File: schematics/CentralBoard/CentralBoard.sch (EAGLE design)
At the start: 10 parts, among them CON1 XT30UPB-M, CON3 XT30UPB-M, IC1 7805T

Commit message: Starting schematics
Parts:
- removed JP1: OD0_Serial, adafruit:PINHD-1X3
- added C10, C11, C12, C13, C14, C15, C9: 2.2uF, rcl:C-EUC1206
- added C17, C2, C4, C7: 100nF, rcl:C-EUC0805
- added CON2, CON4, CON5, CON6, CON7, CON8: XT30UPB-M, amass:XT30UPB-M
- added F1: Fuse 0.2A, fuse:FUSESHK20L
- added IC2: SN75C3232, MAX3232:MAX3232
- added IC3: LTC7001, LTC7001:LTC7001
- added Q1: BC328, transistor-pnp:BC328
- added R3: 4m, rcl:R-EU_R2512
- added R4: 10K, rcl:R-EU_R0805
- added R5: 100K, rcl:R-EU_R0805
- added R6, R7: 1K, rcl:R-EU_R0805
- added SJ1, SJ2, SJ3, SJ4: 0, jumper:SJ
- added SV3: IMU, con-lstb:MA06-1
- added U$2: NVMFS6H824NL-D, DIO_NTS1045EMFST1G:NVMFS6H824NL-D
- C1: value (none) -> 1uF; device rcl:CPOL-EUE15-5AXIAL -> rcl:CPOL-EUE2-5
- C3: value (none) -> 4.7uF; device rcl:CPOL-EUE15-5AXIAL -> rcl:C-EUC0805
- C5: value (none) -> 10uF; device rcl:CPOL-EUE2.5-7 -> rcl:CPOL-EUE2-5
- C6: value (none) -> 0.47uF; device rcl:CPOL-EUE2.5-7 -> rcl:C-EUC0805
- D1: device adafruit:1N4004 -> diode:1N4004
- IC1: value 7805T -> R-78C05.0; device adafruit:7805T -> v-reg:78XXS
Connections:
- removed net RX1: JP1.1, U$1.0-RX1/CS1/CRX2
- removed net TX1: JP1.2, U$1.1-TX1/MISO1/CTX2
- new net +5V: C5.+, D1.A, IC1.OUT, IC3.VCC, Q1.E, R6.1, U$1.VIN
- new net BATT+: CON1.+, CON3.+, R3.1, SJ1.1
- new net BATT-: C10.2, C11.2, C12.2, C13.2, C14.2, C15.2, C9.2, CON1.-, CON2.-, CON3.-, CON4.-, CON5.-, CON6.-, CON7.-, CON8.-, SJ2.1, SJ4.2
- new net IMU-D+: SV3.4
- new net IMU_D-: SV3.3
- new net IMU_RX: IC2.T1OUT, SV3.6
- new net IMU_TX: IC2.R1IN, SV3.5
- new net IMU_VDD: Q1.C, SV3.2
- new net N$1: C1.+, D1.C, F1.2, IC1.IN
- new net N$10: IC3.INP, R4.2, U$1.30-CRX3
- new net N$11: C2.1, IC2.C2+
- new net N$12: C2.2, IC2.C2-
- new net N$13: C7.1, IC2.V+
- new net N$14: C4.1, IC2.V-
- new net N$15: R4.1, SJ4.1
- new net N$16: C3.1, IC3.BST
- new net N$17: IC3.TGUP, R5.2
- new net N$18: R3.2, U$2.D
- new net N$19: C6.1, IC3.TGDN, R5.1, U$2.G
- new net N$2: IC2.T1IN, U$1.29-TX7
- new net N$20: F1.1, SJ1.2
- new net N$21: C10.1, C11.1, C12.1, C13.1, C14.1, C15.1, C9.1, CON2.+, CON4.+, CON5.+, CON6.+, CON7.+, CON8.+, SJ3.2, U$2.S
- new net N$5: IC2.R1OUT, U$1.28-RX7
- new net N$6: C17.1, IC2.C1+
- new net N$7: R6.2, R7.1, U$1.10-CS/MQSR
- new net N$8: C17.2, IC2.C1-
- new net N$9: IC2.VCC, U$1.3V3-3
- net GND: now also C4.2, C7.2, IC2.GND, IC3.GND, IC3.OVLO, IC3.VCCUV, SJ2.2, SV3.1; no longer C3.-, C6.-, CON1.-, CON3.-, JP1.3
- net N$3: now also Q1.B, R7.2; no longer C1.+, C5.+, D1.A, IC1.VO, U$1.VIN
- net N$4: now also C3.2, C6.2, IC3.TS, SJ3.1; no longer C3.+, C6.+, CON1.+, CON3.+, D1.C, IC1.VI
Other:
- moved on the sheet: C1, C5, CON1, CON3

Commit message: used MAX3232 IC for IMU connection now
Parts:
- removed C3: 4.7uF, rcl:C-EUC0805
- removed F1: Fuse 0.2A, fuse:FUSESHK20L
- removed IC3: LTC7001, LTC7001:LTC7001
- removed R5: 100K, rcl:R-EU_R0805
- removed R6: 1K, rcl:R-EU_R0805
- added D2: 1N4148DO35-7, diode:1N4148DO35-7
- added R1: 10k, rcl:R-EU_R0805
- added U1: LTC4440ES6-5TRMSOP8P, LTC4440ES6-5TR:LTC4440ES6-5TRMSOP8P
- U$2: value NVMFS6H824NL-D -> DMTH8003SPS
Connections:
- removed net N$16: C3.1, IC3.BST
- removed net N$17: IC3.TGUP, R5.2
- new net N$24: C6.1, D2.C, U1.BOOST
- net +5V: now also D2.A, R1.1, U1.VCC; no longer IC3.VCC, R6.1
- net GND: no longer IC3.GND, IC3.OVLO, IC3.VCCUV
- net N$1: no longer F1.2
- net N$10: now also U1.INP; no longer IC3.INP
- net N$15: now also U1.GND
- net N$19: now also U1.TG; no longer C6.1, IC3.TGDN, R5.1
- net N$20: no longer F1.1
- net N$3: now also R1.2
- net N$4: now also U1.TS; no longer C3.2, IC3.TS
- net N$7: now also U$1.9-OUT1C; no longer R6.2, U$1.10-CS/MQSR
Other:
- moved on the sheet: Q1, R4, R7

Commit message: Added sockets for IMU, Sensors and ODrives
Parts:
- removed D1: 1N4004, diode:1N4004
- removed IC1: R-78C05.0, v-reg:78XXS
- removed Q1: BC328, transistor-pnp:BC328
- removed SV3: IMU, con-lstb:MA06-1
- removed U1: LTC4440ES6-5TRMSOP8P, LTC4440ES6-5TR:LTC4440ES6-5TRMSOP8P
- added C3: 4.7uF, rcl:C-EUC0805
- added C8: 10uF, rcl:C-EUC0805
- added IC3: LTC7001, LTC7001:LTC7001
- added L1: 10uH, rcl:L-EU0204/5
- added LED1: Power, led:LG_T679-E1F1-1
- added LED2: P-ODrive, led:LG_T679-E1F1-1
- added P10: Power Switch, jst-ph:JST-PH2
- added P11: Foot4, jst-ph:JST-PH3
- added P12: Foot3, jst-ph:JST-PH3
- added P13: Foot2, jst-ph:JST-PH3
- added P14: Foot1, jst-ph:JST-PH3
- added P2: ODrive1, jst-ph:JST-PH3
- added P3: MAIN_SPI, jst-ph:JST-PH4
- added P4: IMU, jst-ph:JST-PH6
- added P5: ODrive2, jst-ph:JST-PH3
- added P6: ODrive3, jst-ph:JST-PH3
- added P7: ODrive4, jst-ph:JST-PH3
- added P8: ODrive5, jst-ph:JST-PH3
- added P9: ODrive6, jst-ph:JST-PH3
- added R10: 100k, rcl:R-EU_R0805
- added R11, R8: 100K, rcl:R-EU_R0805
- added R12, R13: 1K, rcl:R-EU_R0805
- added R2, R5: 2.2K, rcl:R-EU_R0805
- added R6: 10K, rcl:R-EU_R0805
- added R9: 47k, rcl:R-EU_R0805
- added SJ5: 0, jumper:SJ
- added U$3: TLF50211EL, TLF50211EL:TLF50211EL
- added U$4: MCP1725-ADJE/SN, MCP1725-ADJE_SN:MCP1725-ADJE/SN
- added U$5: AP2128-3.3V, AP2128:AP2128-3.3V
- added U2: INA226AIDGST, INA226AIDGST:INA226AIDGST
- C1: device rcl:CPOL-EUE2-5 -> rcl:C-EUC0805
- C5: value 10uF -> 1nF; device rcl:CPOL-EUE2-5 -> rcl:C-EUC0805
- D2: value 1N4148DO35-7 -> 1N4004; device diode:1N4148DO35-7 -> diode:1N4004
- R1: value 10k -> 100K
- R7: value 1K -> 10K
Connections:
- net N$2 renamed T_TX
- net N$5 renamed T_RX
- new net +3.3V: C1.1, P11.2, P12.2, P13.2, P14.2, U$5.OUT
- new net BATT: P10.1, SJ1.2, U$3.VS, U2.IN+, U2.VBUS
- new net CS: P3.4, U$1.10-CS/MQSR
- new net MISO: P3.2, U$1.12-MISO/MQSL
- new net MOSI: P3.3, U$1.11-MOSI/CTX1
- new net N$16: C6.2, R6.2
- new net N$17: R2.1, U$1.19-A5/SCL0, U2.SCL
- new net N$2: LED1.C, R12.2
- new net N$22: R5.1, U$1.18-A4/SDA0, U2.SDA
- new net N$23: R11.2, R2.2, R5.2, U$1.3V3-3, U2.VS
- new net N$25: R1.1, R7.2, U$4.ADJ
- new net N$26: C3.2, IC3.TS, LED2.A, SJ3.1
- new net N$27: R9.2, U$3.FREQ
- new net N$29: D2.C, L1.1, U$3.SWO
- new net N$30: LED2.C, R13.2
- new net N$31: IC2.VCC, P4.5, R1.2, U$4.VOUT
- new net N$5: U$1.31-CTX3, U2.ALERT
- new net O1_RX: P2.2, U$1.0-RX1/CS1/CRX2
- new net O1_TX: P2.3, U$1.1-TX1/MISO1/CTX2
- new net O2_RX: P5.2, U$1.7-RX2/OUT1A
- new net O2_TX: P5.3, U$1.8-TX2/IN1
- new net O3_RX: P6.2, U$1.15-A1/RX3/SPDIF_IN
- new net O3_TX: P6.3, U$1.14-A0/TX3/SPDIF_OUT
- new net O4_RX: P7.2, U$1.16-A2/RX4/SCL1
- new net O4_TX: P7.3, U$1.17-A3/TX4/SDA1
- new net O5_RX: P8.2, U$1.21-A7/RX5/BCLK1
- new net O5_TX: P8.3, U$1.20-A6/TX5/LRCLK1
- new net O6_RX: P9.2, U$1.25-A11/RX6/SDA2
- new net O6_TX: P9.3, U$1.24-A10/TX6/SCL2
- new net SENSOR1: P14.3, U$1.22-A8/CTX1
- new net SENSOR2: P13.3, U$1.23-A9/CRX1/MCLK1
- new net SENSOR3: P12.3, U$1.38-A14/CS/IN1
- new net SENSOR4: P11.3, U$1.39-A15/CS/OUT1A
- net +5V: now also C8.1, IC3.VCC, L1.2, LED1.A, U$3.FB, U$4.VIN, U$5.IN; no longer C5.+, D1.A, D2.A, IC1.OUT, Q1.E, R1.1, U$1.VIN, U1.VCC
- net GND: now also C1.2, C5.2, C8.2, D2.A, P11.1, P12.1, P13.1, P14.1, P2.1, P3.1, P4.6, P5.1, P6.1, P7.1, P8.1, P9.1, R10.1, R12.1, R7.1, R9.1, U$3.GND, U$3.SYNC, U$4.GND, U$5.GND, U2.A0, U2.A1, U2.GND; no longer C1.-, C5.-, IC1.GND, SV3.1
- net IMU-D+: now also P4.3; no longer SV3.4
- net IMU_D-: now also P4.4; no longer SV3.3
- net IMU_RX: now also P4.1; no longer SV3.6
- net IMU_TX: now also P4.2; no longer SV3.5
- net IMU_VDD: now also R11.1, U$1.32-OUT1B, U$4.PWRGD; no longer Q1.C, SV3.2
- net N$1: now also U$1.VIN; no longer C1.+, D1.C, IC1.IN
- net N$10: now also IC3.INP; no longer U1.INP
- net N$15: now also IC3.GND, IC3.OVLO, IC3.VCCUV, R13.1, R6.1; no longer U1.GND
- net N$18: now also SJ5.1, U2.IN-; no longer R3.2, U$2.D
- net N$19: now also C6.1, IC3.TGDN, R8.1; no longer U1.TG
- net N$20: now also P10.2, R10.2, U$3.EN; no longer SJ1.2
- net N$24: now also C3.1, IC3.BST; no longer C6.1, D2.C, U1.BOOST
- net N$3: now also C5.1, U$4.CDELAY; no longer Q1.B, R1.2, R7.2
- net N$4: now also IC3.TGUP, R8.2; no longer C6.2, SJ3.1, U1.TS
- net N$7: now also U$4.!SHDN; no longer R7.1
- net N$9: now also R3.2, SJ5.2, U$2.D; no longer IC2.VCC, U$1.3V3-3
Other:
- moved on the sheet: C6, CON1, CON3, R1, R3, R7, SJ1, SJ2

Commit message: removed old SMD version
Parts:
- removed C1: 1uF, rcl:C-EUC0805
- removed C5: 1nF, rcl:C-EUC0805
- removed C8: 10uF, rcl:C-EUC0805
- removed D2: 1N4004, diode:1N4004
- removed LED1: Power, led:LG_T679-E1F1-1
- removed LED2: P-ODrive, led:LG_T679-E1F1-1
- removed R9: 47k, rcl:R-EU_R0805
- added C16: 2.2uF, rcl:CPOL-EUE2-5
- added C18: 100nF, rcl:C-EU025-025X050
- added C19: 4.7uF, rcl:C-EU025-025X050
- added D1: (no value), adafruit:SCHOTTKY-DIODEDO41
- added LED3: P-ODrive, adafruit:LED3MM
- added LED4: ON, adafruit:LED3MM
- added P1: Foot1, jst-ph:JST-PH3
- added R15: 1k, rcl:R-EU_0204/7
- C10, C11, C12, C13, C14, C9: device rcl:C-EUC1206 -> rcl:CPOL-EUE2-5
- C15: value 2.2uF -> 0.47uF#; device rcl:C-EUC1206 -> rcl:C-EU025-025X050
- C17: value 100nF -> 10uF; device rcl:C-EUC0805 -> rcl:CPOL-EUE2-4
- C2, C4: device rcl:C-EUC0805 -> rcl:C-EU025-025X050
- C3: value 4.7uF -> 100nF; device rcl:C-EUC0805 -> rcl:C-EU025-025X050
- C6: value 0.47uF -> 1uF; device rcl:C-EUC0805 -> rcl:CPOL-EUE2-4
- C7: value 100nF -> 1nF; device rcl:C-EUC0805 -> rcl:C-EU025-025X050
- P10: value Power Switch -> Switch
- P11: value Foot4 -> Foot2
- P13: value Foot2 -> Foot4
- P14: value Foot1 -> SPI2; device jst-ph:JST-PH3 -> jst-ph:JST-PH4
- P3: value MAIN_SPI -> SPI
- R1: value 100K -> 10K; device rcl:R-EU_R0805 -> rcl:R-EU_0204/7
- R10, R13, R2, R5: device rcl:R-EU_R0805 -> rcl:R-EU_0204/7
- R11: value 100K -> 100k; device rcl:R-EU_R0805 -> rcl:R-EU_0204/7
- R12: value 1K -> 100k; device rcl:R-EU_R0805 -> rcl:R-EU_0204/7
- R4: value 10K -> 10k; device rcl:R-EU_R0805 -> rcl:R-EU_0204/7
- R6: value 10K -> 100k; device rcl:R-EU_R0805 -> rcl:R-EU_0204/7
- R7: value 10K -> 47k; device rcl:R-EU_R0805 -> rcl:R-EU_0204/7
- R8: value 100K -> 10; device rcl:R-EU_R0805 -> rcl:R-EU_0204/7
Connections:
- net SENSOR3 renamed SENS3
- removed net SENSOR1: P14.3, U$1.22-A8/CTX1
- removed net SENSOR2: P13.3, U$1.23-A9/CRX1/MCLK1
- removed net SENSOR4: P11.3, U$1.39-A15/CS/OUT1A
- new net CS1: P14.4, U$1.40-A16/CS1
- new net MISO1: P14.2, U$1.41-A17/MISO1
- new net MOSI1: P14.3, U$1.26-A12/MOSI1
- new net SCK1: U$1.27-A13/SCK1
- new net SENS1: P1.3, U$1.22-A8/CTX1
- new net SENS2: P11.3, U$1.23-A9/CRX1/MCLK1
- new net SENS4: P13.3, U$1.39-A15/CS/OUT1A
- net +3.3V: now also C6.+, P1.2; no longer C1.1, P14.2
- net +5V: now also C17.+, LED4.A; no longer C8.1, LED1.A
- net BATT-: now also C10.-, C11.-, C12.-, C13.-, C14.-, C16.-, C9.-; no longer C10.2, C11.2, C12.2, C13.2, C14.2, C15.2, C9.2
- net GND: now also C17.-, C3.2, C6.-, D1.A, P1.1, R1.2, R13.2; no longer C1.2, C5.2, C8.2, D2.A, R10.1, R9.1
- net IMU_VDD: now also R6.1; no longer R11.1
- net N$10: now also R4.1; no longer R4.2
- net N$13: now also C4.1; no longer C7.1
- net N$14: now also C3.1; no longer C4.1
- net N$15: now also R15.2, R4.2, R8.2; no longer R13.1, R4.1, R6.1
- net N$16: now also C15.2, R8.1; no longer C6.2, R6.2
- net N$17: now also R5.2; no longer R2.1
- net N$19: now also C15.1, R10.2; no longer C6.1, R8.1
- net N$2: now also LED4.C, R13.1; no longer LED1.C, R12.2
- net N$20: now also R12.2; no longer R10.2
- net N$21: now also C10.+, C11.+, C12.+, C13.+, C14.+, C16.+, C9.+; no longer C10.1, C11.1, C12.1, C13.1, C14.1, C15.1, C9.1
- net N$22: now also R2.2; no longer R5.1
- net N$23: now also R2.1, R5.1, R6.2; no longer R11.2, R2.2, R5.2
- net N$24: now also C19.1; no longer C3.1
- net N$25: now also R11.2; no longer R7.2
- net N$26: now also C19.2, LED3.A; no longer C3.2, LED2.A
- net N$27: now also R7.2; no longer R9.2
- net N$29: now also D1.C; no longer D2.C
- net N$3: now also C7.1; no longer C5.1
- net N$30: now also LED3.C, R15.1; no longer LED2.C, R13.2
- net N$31: now also R11.1; no longer R1.2
- net N$4: now also R10.1; no longer R8.2
- net N$6: now also C18.1; no longer C17.1
- net N$8: now also C18.2; no longer C17.2
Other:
- note added: "Foot Sensor, coming in as analogue input"
- note added: "Serial connection to 6 ODrives"
- moved on the sheet: C15, C3, C4, C7, P11, P12, P13, R1, R10, R11, R12, R13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

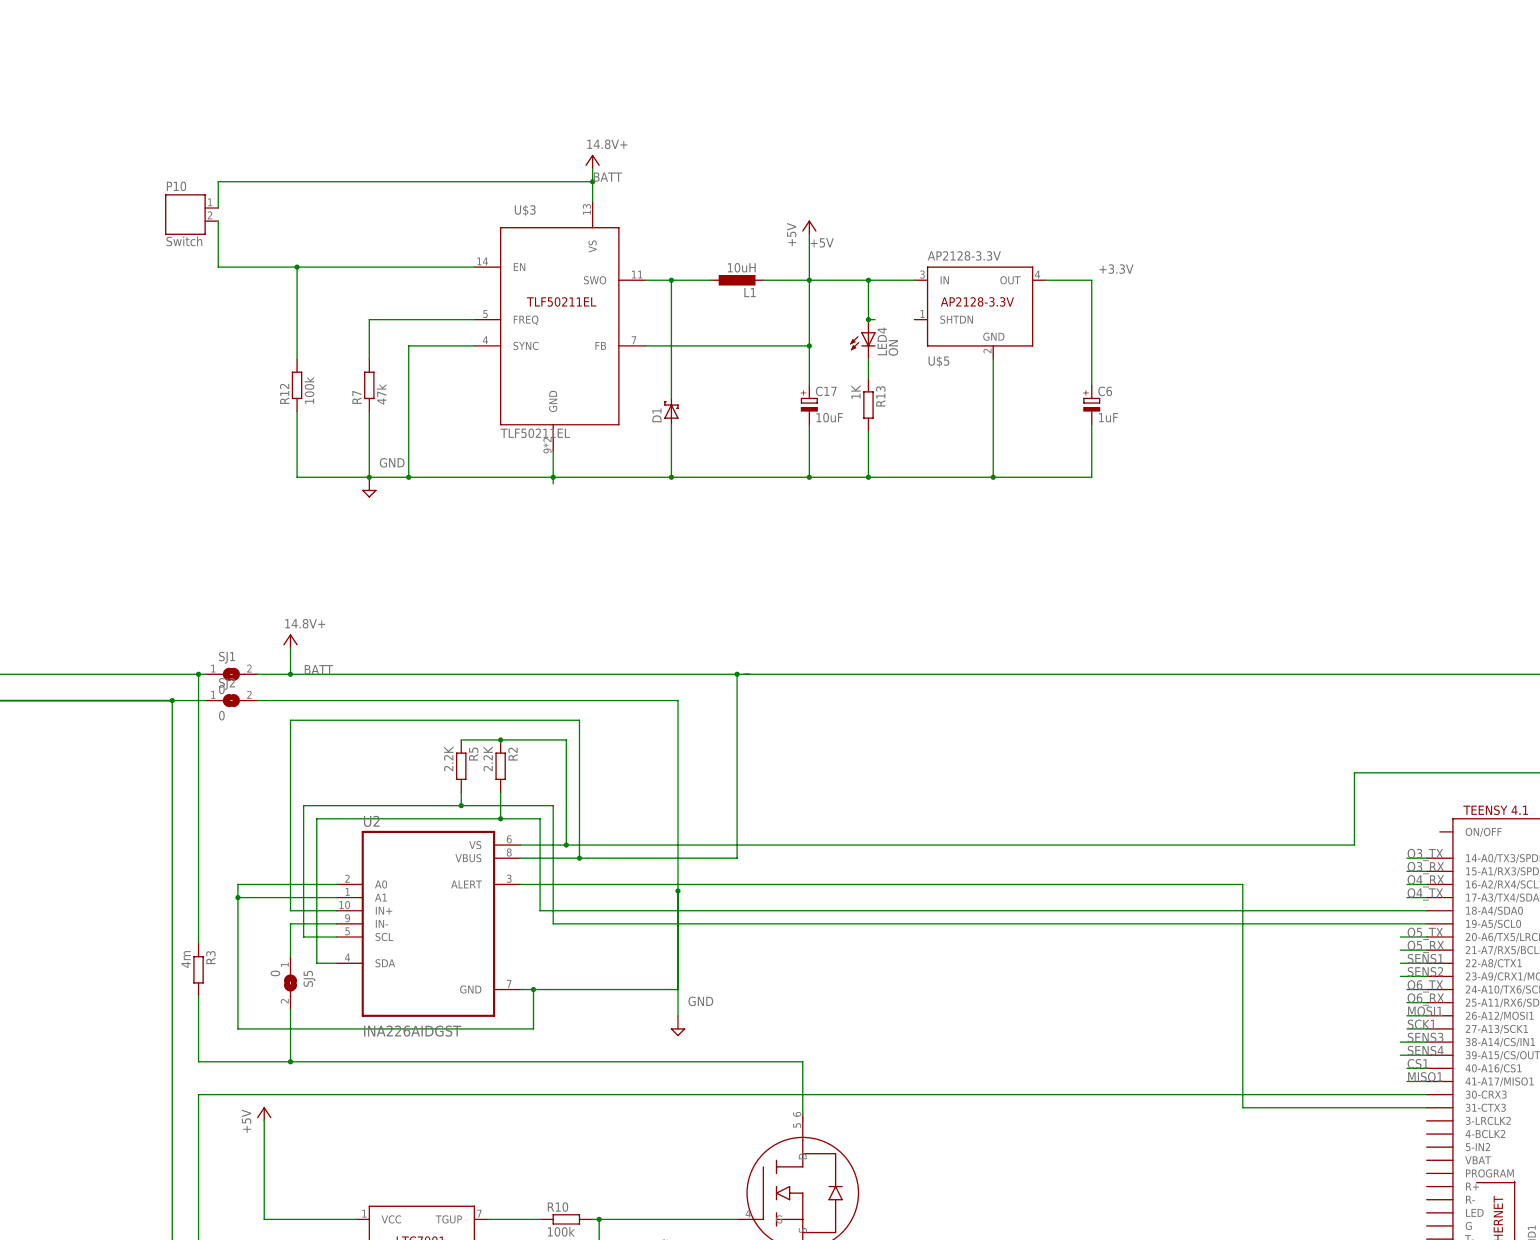
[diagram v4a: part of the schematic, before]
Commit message: new head and tail
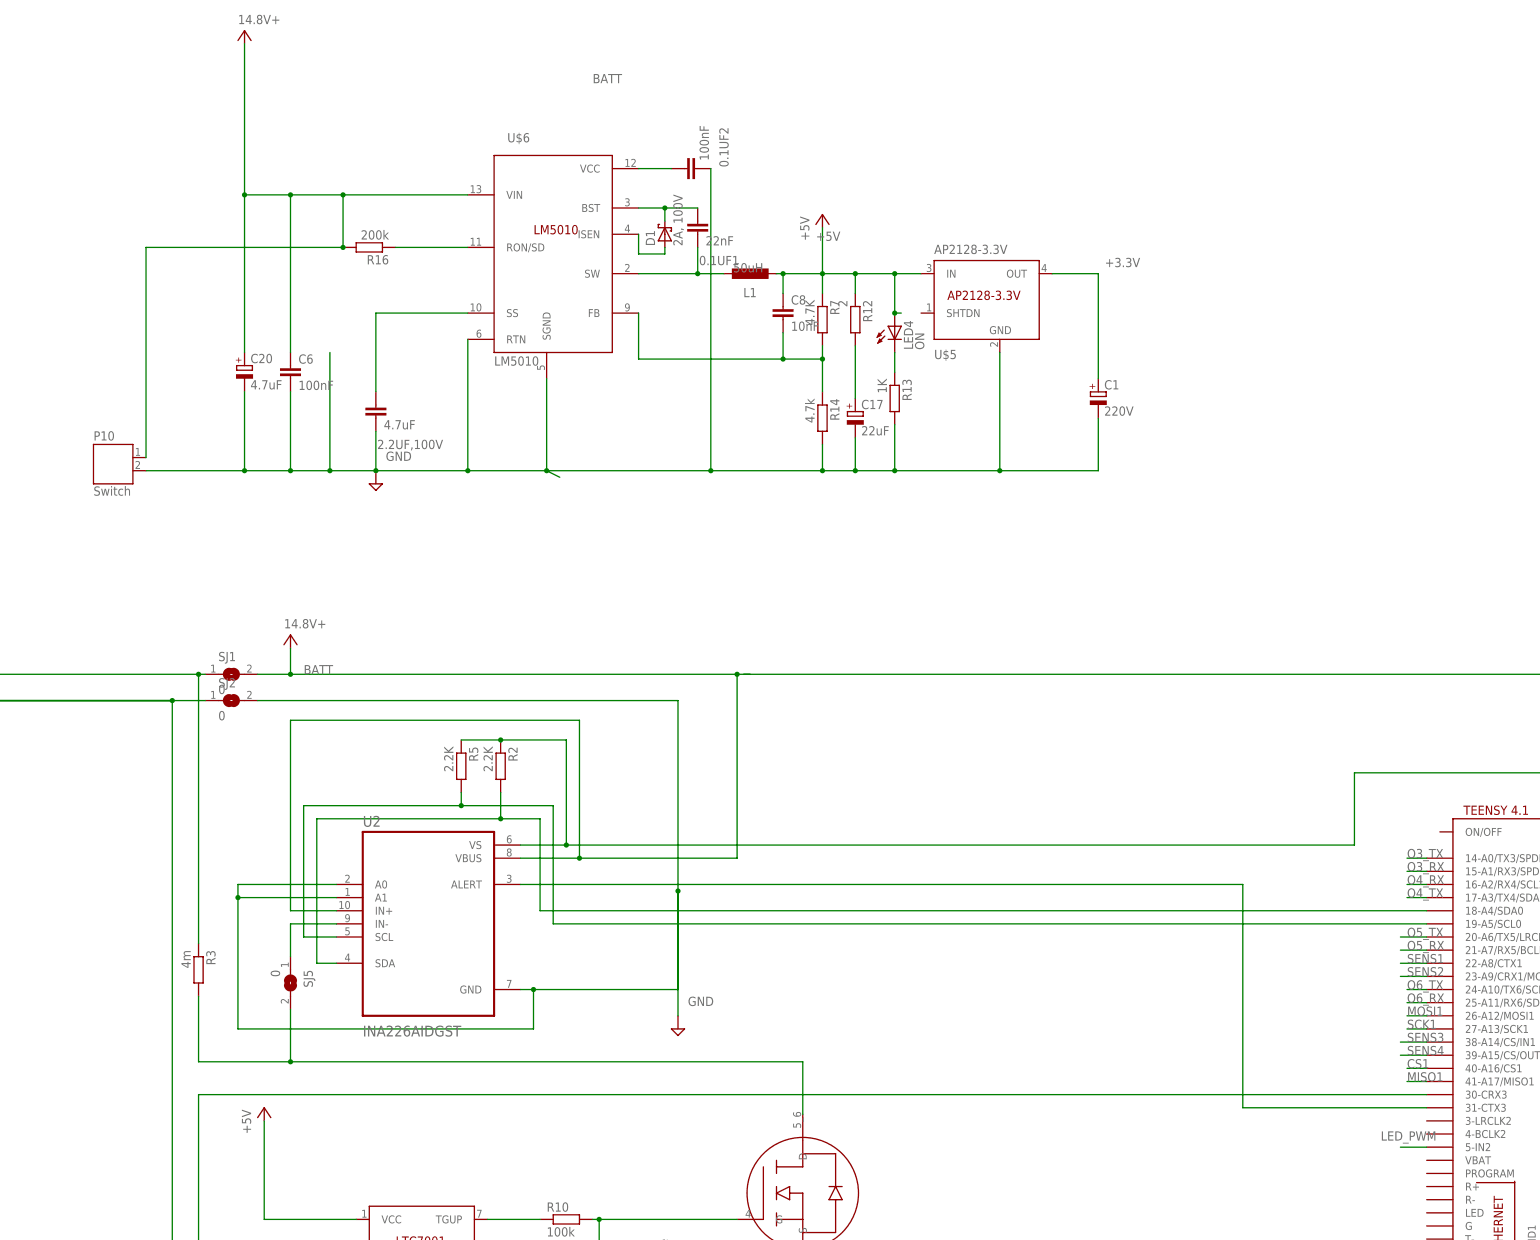
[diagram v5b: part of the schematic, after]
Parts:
- removed U$3: TLF50211EL, TLF50211EL:TLF50211EL
- added 0.1UF1: 22nF, rcl:C-EU025-025X050
- added 0.1UF2: 100nF, rcl:C-EU025-025X050
- added 2.2UF,100V: 4.7uF, rcl:C-EU025-025X050
- added C1: 220V, rcl:CPOL-EUE2.5-7
- added C20: 4.7uF, rcl:CPOL-EUE2-4
- added C8: 10nF, rcl:C-EU025-025X050
- added R14: 4.7k, rcl:R-EU_0204/7
- added R16: 200k, rcl:R-EU_0204/7
- added U$6: LM5010, LM5010:LM5010
- C17: value 10uF -> 22uF
- C6: value 1uF -> 100nF; device rcl:CPOL-EUE2-4 -> rcl:C-EU025-025X050
- D1: value (none) -> 2A, 100V
- L1: value 10uH -> 50uH
- R12: value 100k -> 2
- R7: value 47k -> 4.7K
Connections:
- new net LED_PWM: U$1.5-IN2
- new net N$33: 2.2UF,100V.1, U$6.SS
- new net N$34: 0.1UF2.1, U$6.VCC
- new net N$35: 0.1UF1.2, L1.1, U$6.SW
- new net N$36: C8.2, R14.1, R7.2, U$6.FB
- new net N$37: D1.A, U$6.ISEN
- net +3.3V: now also C1.+; no longer C6.+
- net +5V: now also C8.1, R12.1, R7.1; no longer C17.+, U$3.FB
- net BATT: now also C20.+, C6.1, R16.2, U$6.VIN; no longer U$3.VS
- net GND: now also 0.1UF2.2, 2.2UF,100V.2, C1.-, C20.-, C6.2, P10.2, R14.2, U$6.RTN, U$6.SGND; no longer C6.-, D1.A, R12.1, R7.1, U$3.GND, U$3.SYNC
- net N$20: now also C17.+; no longer P10.2, U$3.EN
- net N$27: now also R16.1, U$6.RON/SD; no longer R7.2, U$3.FREQ
- net N$29: now also 0.1UF1.1, U$6.BST; no longer L1.1, U$3.SWO
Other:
- moved on the sheet: C17, D1, L1, LED4, P10, R12, R13, R7, U$5
